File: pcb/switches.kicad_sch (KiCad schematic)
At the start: 4 parts, among them U2 SN74LVC245APW, U3 SN74LVC245APW

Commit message: fixes #5
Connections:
- net Switch 3/SW: now also U3.9 (A8); no longer U3.8 (A7)
- net Switch 4/SW: now also U3.8 (A7); no longer U3.9 (A8)
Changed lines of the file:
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@@
 			(color 0 0 0 0.0000)
 		)
-		(property "Sheetname" "Switch 3"
+		(property "Sheetname" "Switch 4"
 			(at 158.75 123.7484 0)
 			(effects
@@
 			(color 0 0 0 0.0000)
 		)
-		(property "Sheetname" "Switch 4"
+		(property "Sheetname" "Switch 3"
 			(at 158.75 135.1784 0)
 			(effects

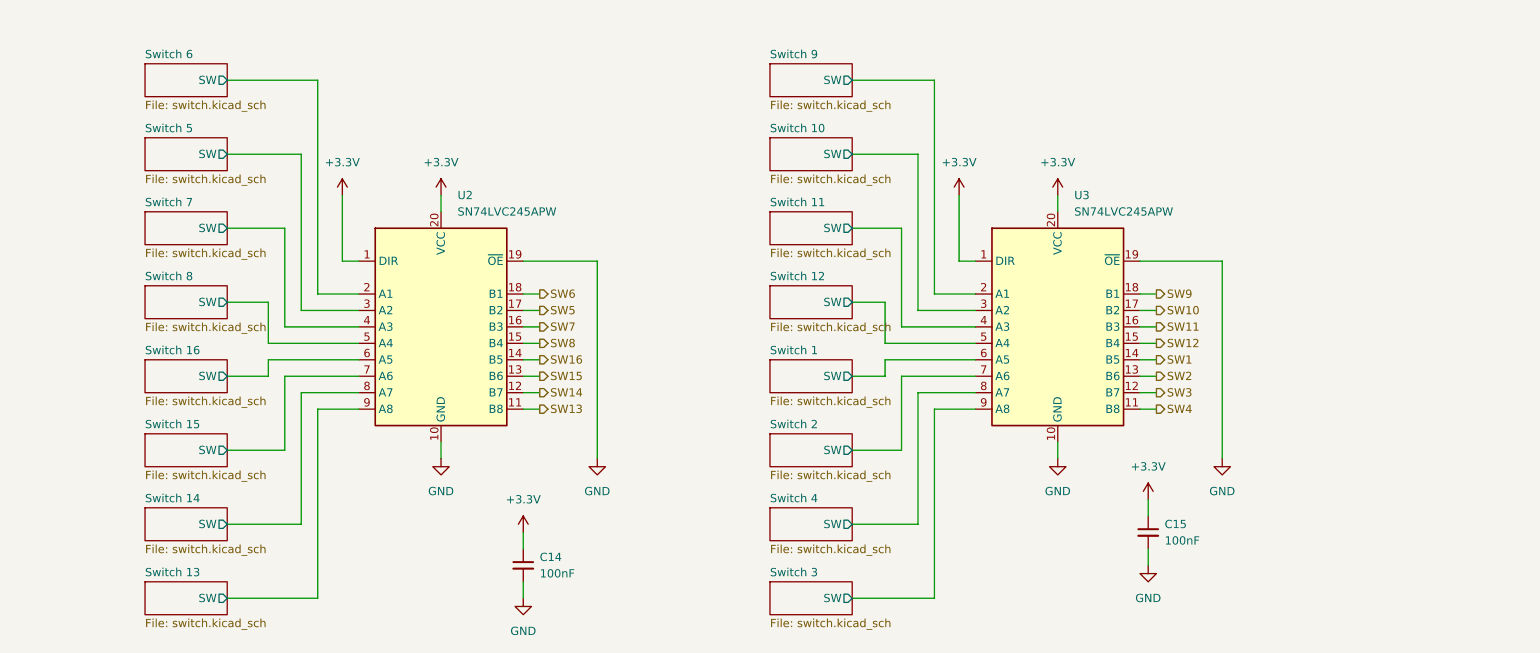
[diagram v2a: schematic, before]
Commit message: fixes #12
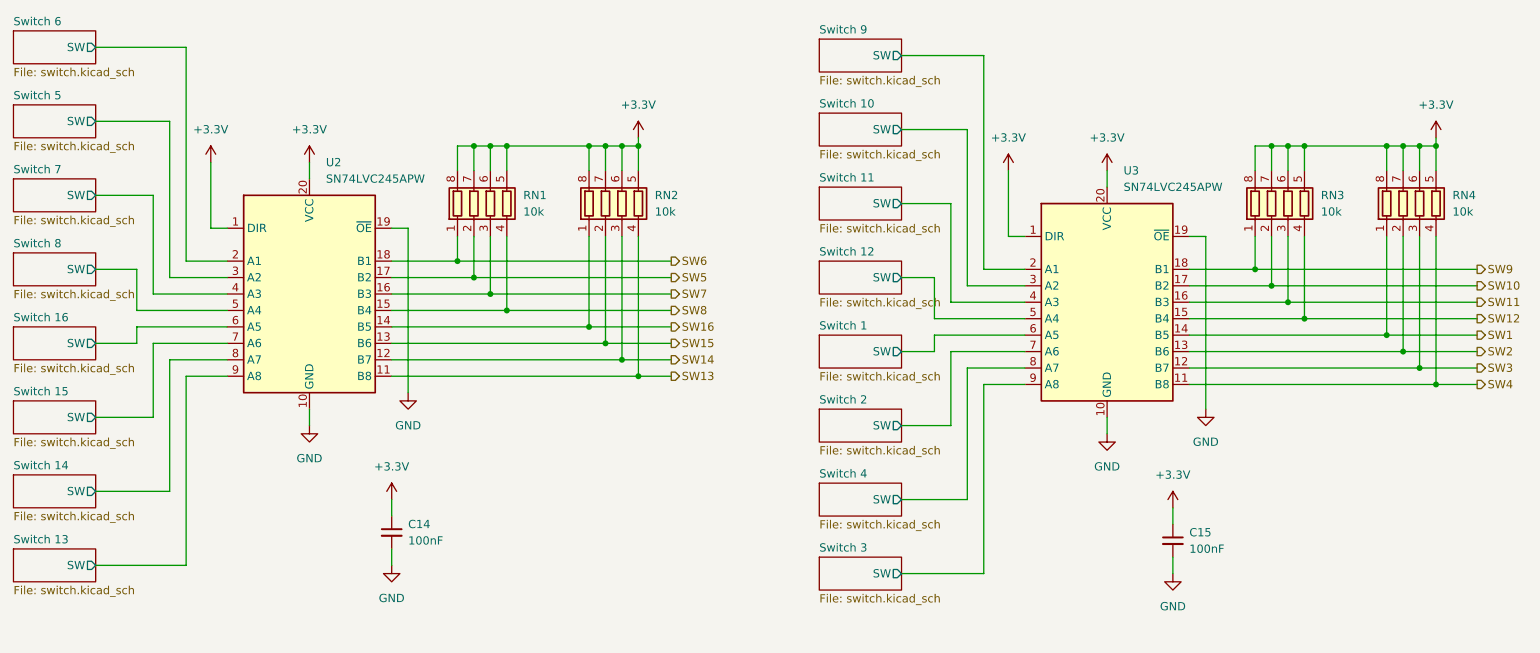
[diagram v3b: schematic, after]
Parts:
- added RN1, RN2, RN3, RN4: 10k, Resistor_SMD:R_Array_Convex_4x0603, symbol Device:R_Pack04
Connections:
- net +3.3V: now also RN1.5 (R4.2), RN1.6 (R3.2), RN1.7 (R2.2), RN1.8 (R1.2), RN2.5 (R4.2), RN2.6 (R3.2), RN2.7 (R2.2), RN2.8 (R1.2), RN3.5 (R4.2), RN3.6 (R3.2), RN3.7 (R2.2), RN3.8 (R1.2), RN4.5 (R4.2), RN4.6 (R3.2), RN4.7 (R2.2), RN4.8 (R1.2)
- net SW1: now also RN4.1 (R1.1)
- net SW10: now also RN3.2 (R2.1)
- net SW11: now also RN3.3 (R3.1)
- net SW12: now also RN3.4 (R4.1)
- net SW13: now also RN2.4 (R4.1)
- net SW14: now also RN2.3 (R3.1)
- net SW15: now also RN2.2 (R2.1)
- net SW16: now also RN2.1 (R1.1)
- net SW2: now also RN4.2 (R2.1)
- net SW3: now also RN4.3 (R3.1)
- net SW4: now also RN4.4 (R4.1)
- net SW5: now also RN1.2 (R2.1)
- net SW6: now also RN1.1 (R1.1)
- net SW7: now also RN1.3 (R3.1)
- net SW8: now also RN1.4 (R4.1)
- net SW9: now also RN3.1 (R1.1)
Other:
- moved on the sheet: C14, C15, U2, U3

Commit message: specified some values and colors added lcsc part ids for all components
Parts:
- C14, C15: LCSC (none) -> C14663
- RN1, RN2, RN3, RN4: LCSC (none) -> C29718
- U2, U3: LCSC (none) -> C7848
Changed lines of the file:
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@@
+			)
+		)
+		(property "LCSC" "C14663"
+			(at 102.87 127.0063 0)
+			(effects
+				(font
+					(size 1.27 1.27)
+				)
+				(hide yes)
 			)
 		)
@@
 			)
 		)
+		(property "LCSC" "C29718"
+			(at 264.16 76.1999 0)
+			(effects
+				(font
+					(size 1.27 1.27)
+				)
+				(hide yes)
+			)
+		)
 		(pin "5"
 		)
@@
 			)
 		)
+		(property "LCSC" "C29718"
+			(at 243.84 76.1999 0)
+			(effects
+				(font
+					(size 1.27 1.27)
+				)
+				(hide yes)
+			)
+		)
 		(pin "5"
 		)
@@
 			)
 		)
+		(property "LCSC" "C7848"
+			(at 90.1718 71.12 0)
+			(effects
+				(font
+					(size 1.27 1.27)
+				)
+				(hide yes)
+			)
+		)
 		(pin "17"
 		)
@@
 			)
 		)
+		(property "LCSC" "C7848"
+			(at 213.3618 72.39 0)
+			(effects
+				(font
+					(size 1.27 1.27)
+				)
+				(hide yes)
+			)
+		)
 		(pin "17"
 		)
@@
 			)
 		)
+		(property "LCSC" "C14663"
+			(at 223.52 128.2763 0)
+			(effects
+				(font
+					(size 1.27 1.27)
+				)
+				(hide yes)
+			)
+		)
 		(pin "1"
 		)
@@
 			)
 		)
+		(property "LCSC" "C29718"
+			(at 140.97 76.1999 0)
+			(effects
+				(font
+					(size 1.27 1.27)
+				)
+				(hide yes)
+			)
+		)
 		(pin "5"
 		)
@@
 			(effects
 				(font
+					(size 1.27 1.27)
+				)
+				(hide yes)
+			)
+		)
+		(property "LCSC" "C29718"
+			(at 120.65 76.1999 0)
+			(effects
+				(font
